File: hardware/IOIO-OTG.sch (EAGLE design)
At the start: 60 parts, among them Q1 IRLML2244, Q2 2N7002PW, Q3 AO3404A, U1 PIC24FJ256GB206, U14 SWITCH_SPDT, U2 TPS62133RGTT, U3 VREG_MIC5216

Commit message: copied from v22b @ commit: 'Seed Logo'
needed to copy in v22b, because a lot of work was done to v22b, and we
want to keep these two branches parallel
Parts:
- removed JP18: (no value), SparkFun-Connectors:USB_MICROB_PLUGCONN-11752
- removed LOGO2: SFE_LOGO_FLAME.1_INCH, SparkFun-Aesthetics:SFE_LOGO_FLAME.1_INCH
- removed LOGO4: SFE_LOGO_NAME_FLAME.1_INCH, SparkFun-Aesthetics:SFE_LOGO_NAME_FLAME.1_INCH
- added JP21: AB MICRO USB, SparkFun-Connectors:USB-ABCONN-11794
- C10: device SparkFun-Passives:CAP_POL1206 -> SparkFun-Capacitors:10UF-16V-10%(TANT)
- C11: device SparkFun-Passives:CAP1210 -> SparkFun-Capacitors:10UF50V20%(1210)
- C6: device SparkFun-Passives:CAP0805 -> SparkFun-Capacitors:10UF10V10%(0805)
- C7: device SparkFun:CAP_POL1206 -> SparkFun-Capacitors:10UF-16V-10%(TANT)
- D1: device SparkFun-DiscreteSemi:DIODE-SCHOTTKY_ -> SparkFun-DiscreteSemi:DIODE-SCHOTTKY-B340A
- D2: device IOIO-OTG:SPARKFUN-DISCRETESEMI_DIODE-SCHOTTKY -> SparkFun-DiscreteSemi:DIODE-ZENERDZ2J150M0L
- F1: value PTCSMD -> 0.75A
- JP1: value VIN -> (none)
- JP19: value JST Connector -> JST; device SparkFun:M02-JST-2MM-SMT -> SparkFun-Connectors:JST_2MM_MALE
- JP4: value 5V -> (none)
- L2: device SparkFun-Passives:INDUCTORCR54 -> SparkFun-Passives:INDUCTORCR54-3.3UH
- Q1: device SparkFun-DiscreteSemi:MOSFET-PCHANNELSMD -> SparkFun-DiscreteSemi:MOSFET-PCHANNELIRLML2244
- Q2: device SparkFun-DiscreteSemi:MOSFET-NCHANNELSOT323 -> SparkFun-DiscreteSemi:MOSFET-NCHANNEL2N7002PW
- Q3: value AO3404A -> MOSFET-NCHANNELAO3404A; device IOIO-OTG:SPARKFUN-DISCRETESEMI_MOSFET-NCHANNELSMD -> SparkFun-DiscreteSemi:MOSFET-NCHANNELAO3404A; PART# DMN3404L -> AO3404A
- U1: device SparkFun-DigitalIC:PIC24FXXXDAX06 -> SparkFun-DigitalIC:PIC24FXXXGPX06
- U2: device SparkFun-PowerIC:TPS6214X -> SparkFun-PowerIC:TPS62133RGTT""
- U3: value VREG_MIC5216 -> MIC5216; device SparkFun-PowerIC:VREG_MIC5216 -> SparkFun-PowerIC:V_REG_MIC5216
- renumbered LED1 to D3, LED2 to D5, U$2 to JP20, U14 to S1
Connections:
- net ANCHOR1: now also JP21.SHIELD; no longer JP18.SHIELD
- net D+: now also JP21.D+; no longer JP18.D+
- net D-: now also JP21.D-; no longer JP18.D-
- net GND: now also JP19.-, JP21.GND; no longer JP18.GND, JP19.1
- net USBID: now also JP21.USBID; no longer JP18.ID
- net VBUS: now also JP21.VBUS; no longer JP18.VCC
- net VIN: now also JP19.+; no longer JP19.2
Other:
- note added: "V22b"
- note added: "revised by A.Weiss, Pete Lewis"
- note removed: "V22a"
- note removed: "revised by A.Weiss"
- moved on the sheet: C10, C11, C6, C7, C8, C9, JP3, L2, Q1, Q2, Q3, R1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

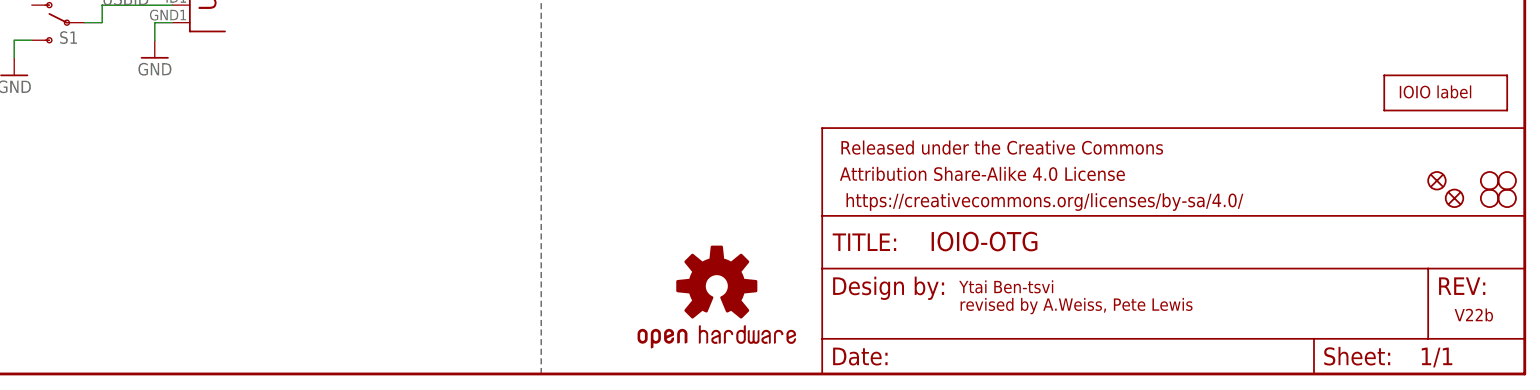
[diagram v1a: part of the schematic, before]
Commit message: SparkFun Logo
Also, changed to v22a in schematic (it was still v22b from the copy
over)
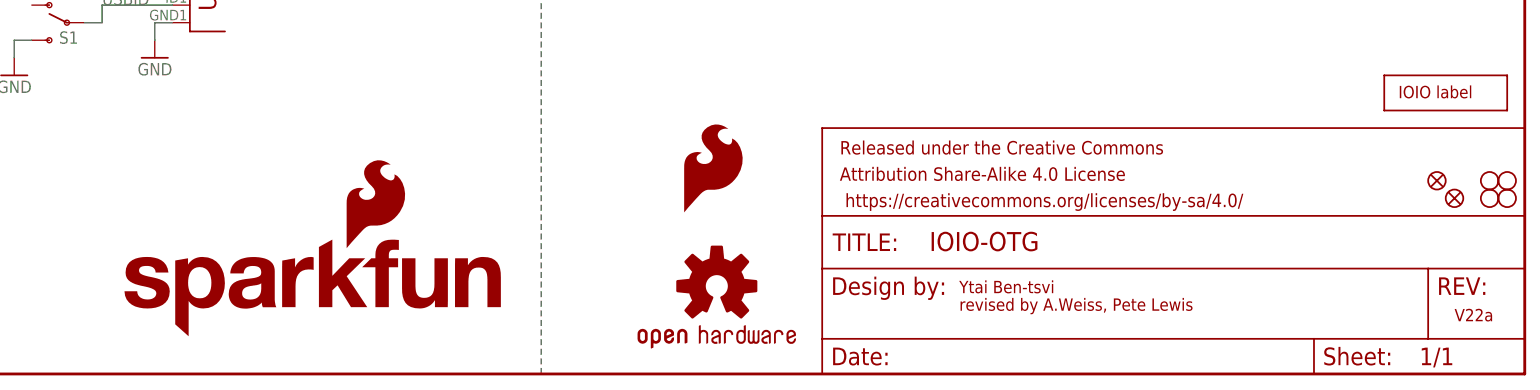
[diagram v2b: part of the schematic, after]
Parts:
- added LOGO2: SFE_LOGO_NAME_FLAME.1_INCH, SparkFun-Aesthetics:SFE_LOGO_NAME_FLAME.1_INCH
- added LOGO3: SFE_LOGO_FLAME.1_INCH, SparkFun-Aesthetics:SFE_LOGO_FLAME.1_INCH
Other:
- note added: "V22a"
- note removed: "V22b"
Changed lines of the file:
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@@
 <part name="JP21" library="SparkFun-Connectors" deviceset="USB-AB" device="CONN-11794" value="AB MICRO USB"/>
 <part name="JP19" library="SparkFun-Connectors" deviceset="JST_2MM_MALE" device="" value="JST"/>
+<part name="LOGO2" library="SparkFun-Aesthetics" deviceset="SFE_LOGO_NAME_FLAME" device=".1_INCH"/>
+<part name="LOGO3" library="SparkFun-Aesthetics" deviceset="SFE_LOGO_FLAME" device=".1_INCH"/>
 </parts>
 <sheets>
@@
 <text x="11.43" y="186.436" size="3.81" layer="97" font="vector">MCU</text>
 <wire x1="289.56" y1="200.66" x2="431.8" y2="200.66" width="0.2032" layer="97" style="shortdash"/>
-<text x="421.64" y="7.62" size="1.778" layer="94" font="vector">V22b</text>
+<text x="421.64" y="7.62" size="1.778" layer="94" font="vector">V22a</text>
 </plain>
 <instances>
@@
 <attribute name="NAME" x="49.022" y="241.3" size="1.778" layer="95" font="vector" rot="R180"/>
 </instance>
+<instance part="LOGO2" gate="G$1" x="228.6" y="5.08"/>
+<instance part="LOGO3" gate="G$1" x="309.88" y="22.86"/>
 </instances>
 <busses>
